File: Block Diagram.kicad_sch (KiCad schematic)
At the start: 0 parts

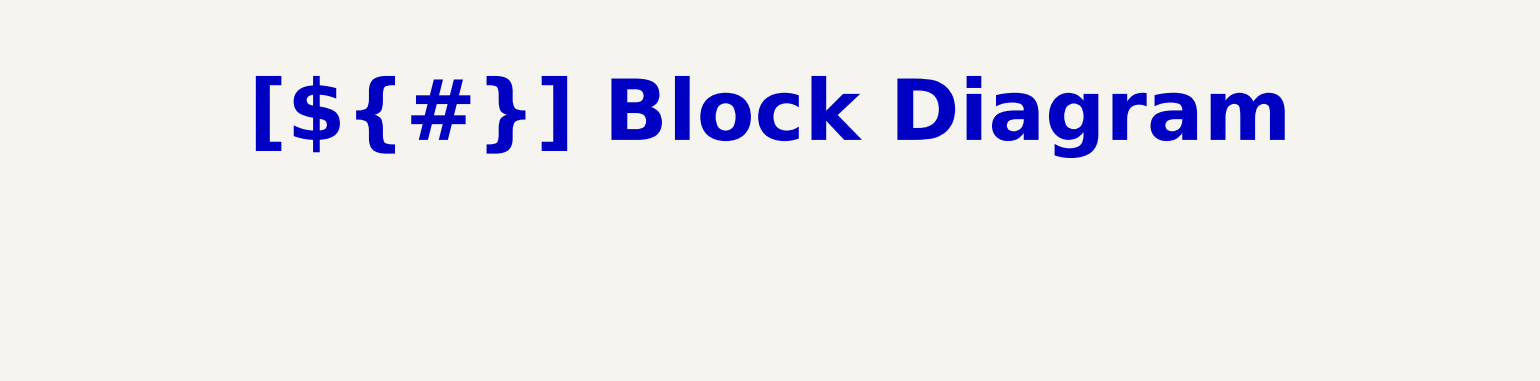
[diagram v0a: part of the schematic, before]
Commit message: test: exercise boardwright preview path
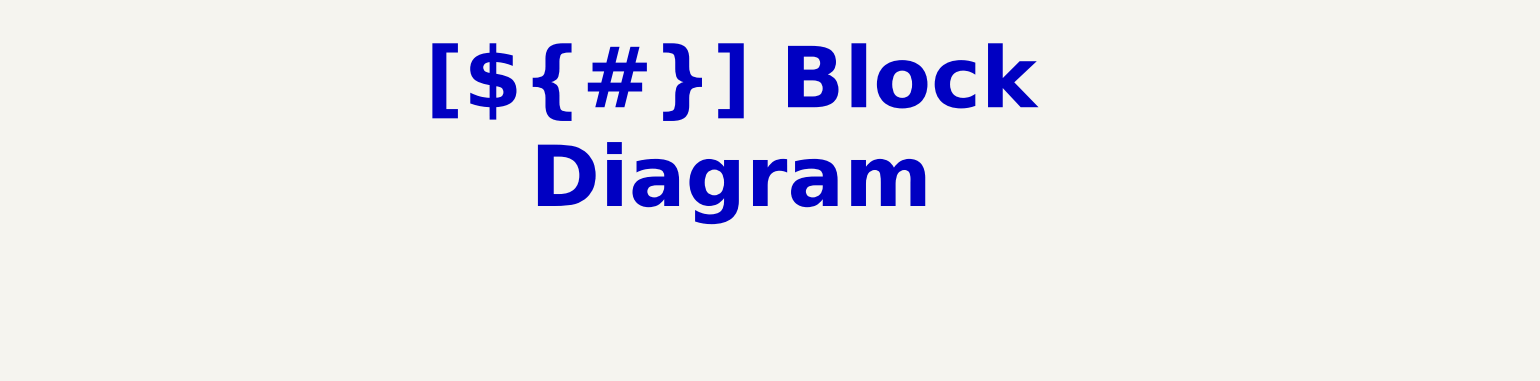
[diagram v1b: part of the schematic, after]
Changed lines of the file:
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@@
 	(text_box "[${#}] ${TITLE}"
 		(exclude_from_sim no)
-		(at 20.32 10.16 0)
-		(size 389.89 20.32)
+		(at 144.78 15 0)
+		(size 130.81 15)
 		(margins 5.9999 5.9999 5.9999 5.9999)
 		(stroke
